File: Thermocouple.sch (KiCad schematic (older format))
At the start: 12 parts, among them U2 MCP3550-60-E/SN, U3 MCP3550-60-E/SN, U4 LM324

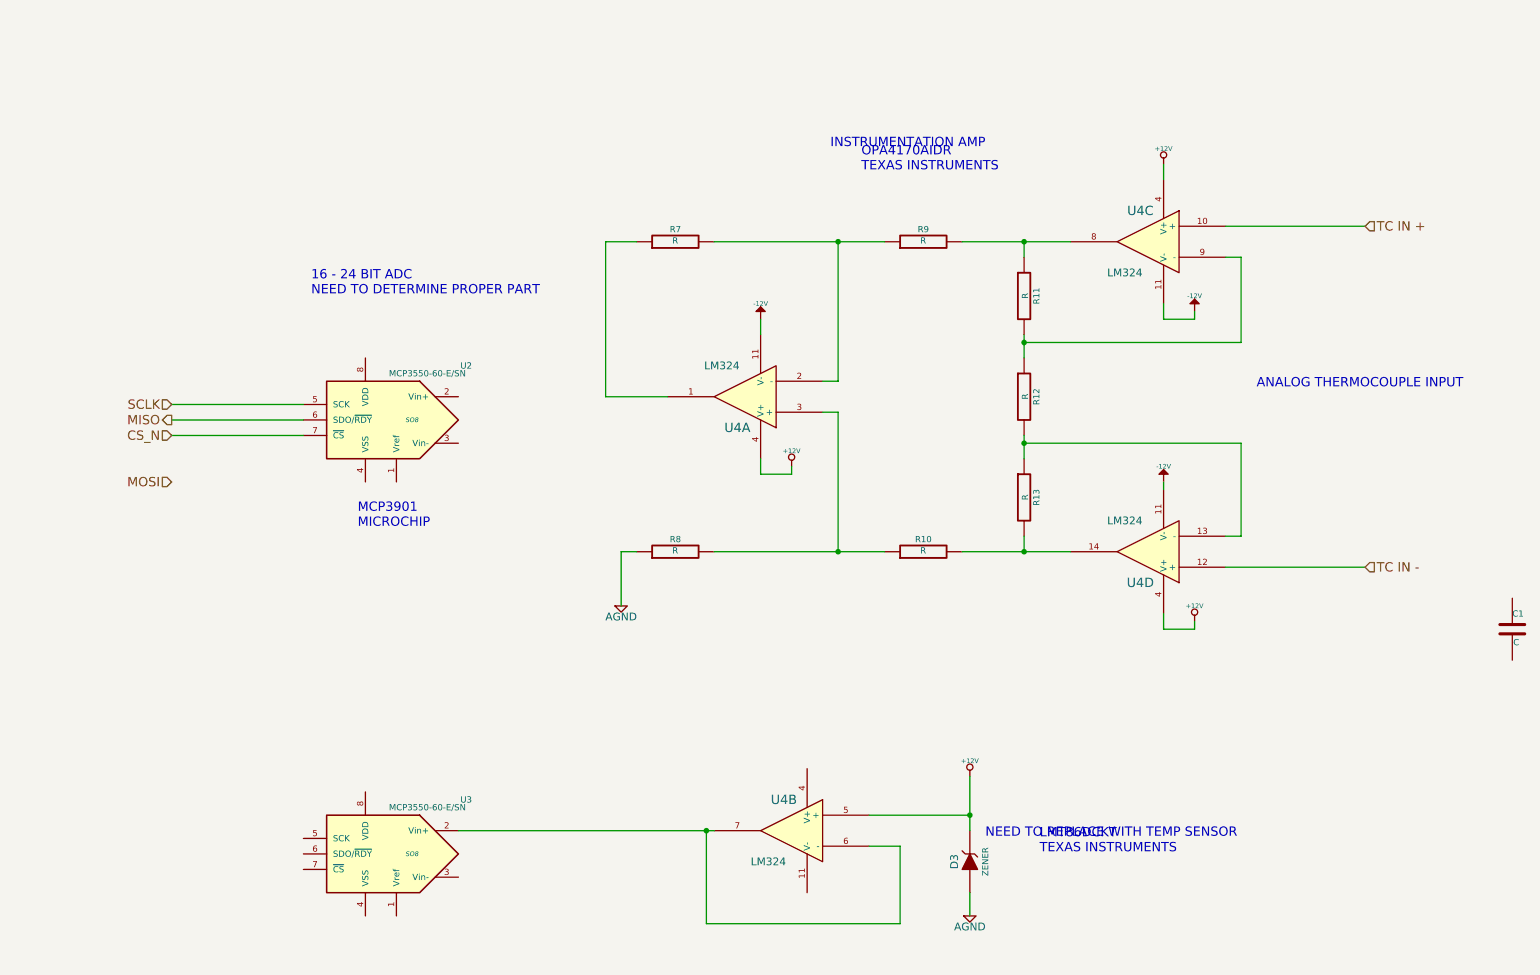
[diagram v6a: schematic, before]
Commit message: worked on associating parts
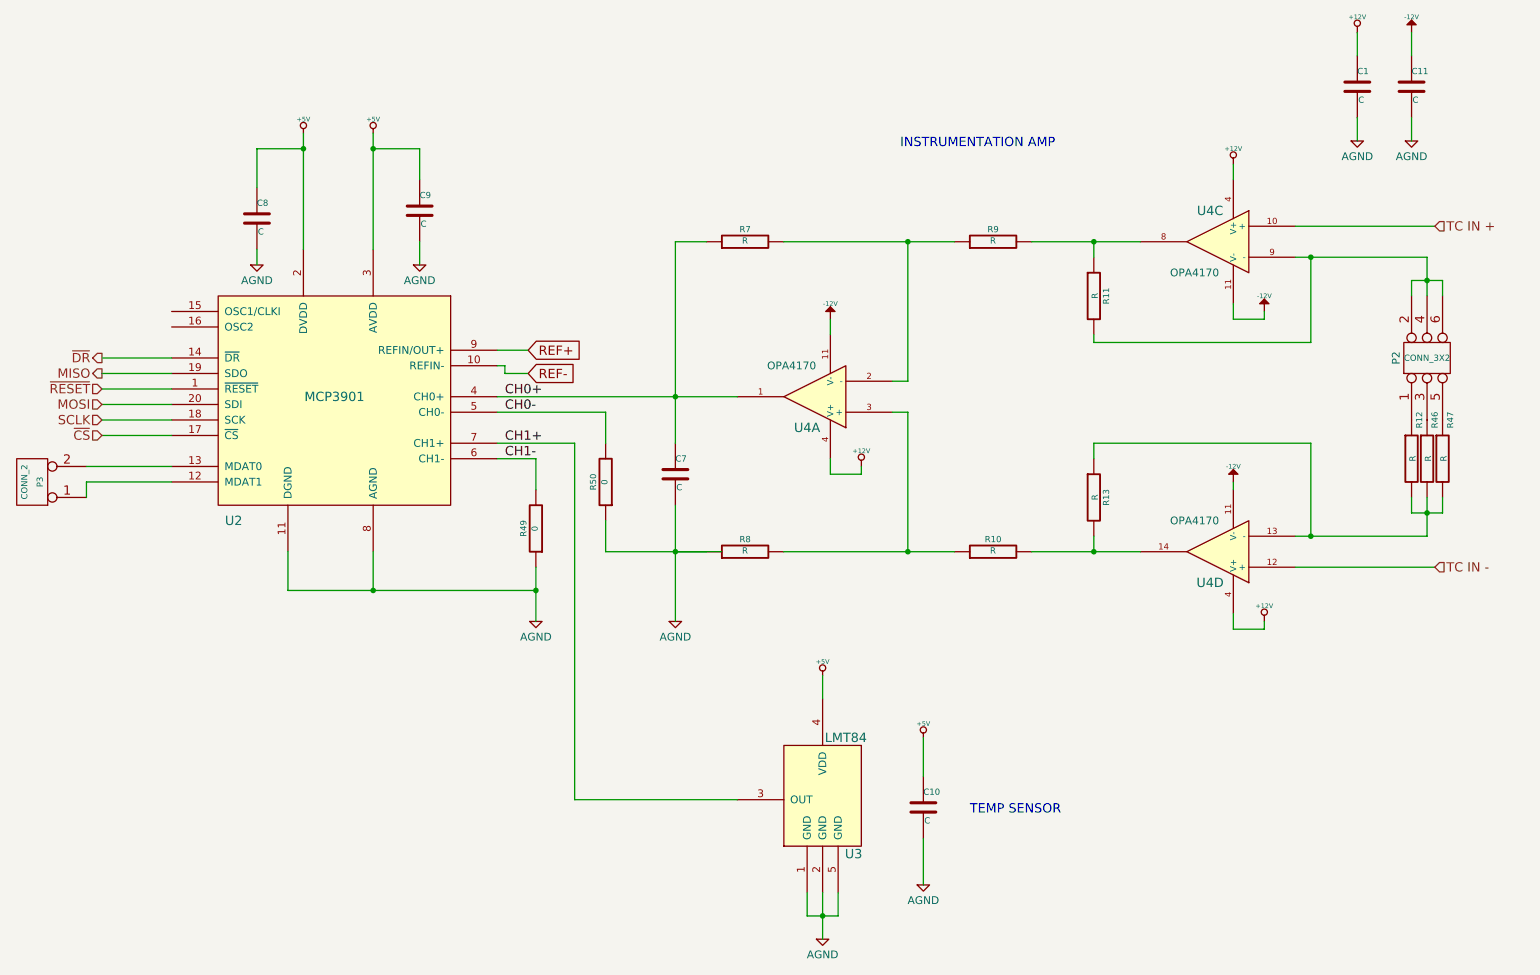
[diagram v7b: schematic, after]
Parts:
- removed D3: ZENER, ~, symbol ZENER
- removed U2, U3: MCP3550-60-E/SN, SO8, symbol MCP3550-60-E/SN
- removed unit 2 of U4
- added C10, C11, C7, C8, C9: C, ~, symbol C
- added P2: CONN_3X2, symbol CONN_3X2
- added P3: CONN_2, symbol CONN_2
- added R46, R47: R, ~, symbol R
- added R49, R50: 0, ~, symbol R
- added U2: MCP3901, symbol MCP3901
- added U3: LMT84, symbol LMT84
- U4: value LM324 -> OPA4170
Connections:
- net +12V: now also C1.1
- net -12V: now also C11.1
- net AGND: now also C1.2, C10.2, C11.2, C7.2, C8.2, C9.2, R49.1, R50.1, U2.11 (DGND), U2.8 (AGND), U3.1 (GND), U3.2 (GND), U3.5 (GND)
- net MISO: now also U2.19 (SDO)
- net MOSI: now also U2.20 (SDI)
- net SCLK: now also U2.18 (SCK)
- net at R11.2, U4.9 (-): now also P2.2, P2.4, P2.6; no longer R12.1
- net at R12.2, R13.1, U4.13 (-): now also R46.2, R47.2
- net CH0+: now reaches R7.1, U4.1
- net CH0+: now also C7.1, U2.4 (CH0+)
- new net: P2.1, R12.1
- new net: P3.1 (P1), U2.12 (MDAT1)
- new net: P3.2 (PM), U2.13 (MDAT0)
- new net: P2.3, R46.1
- new net: P2.5, R47.1
- new net +5V: C10.1, C8.1, C9.1, U2.2 (DVDD), U2.3 (AVDD), U3.4 (VDD)
- new net CH0-: R50.2, U2.5 (CH0-)
- new net CH1+: U2.7 (CH1+), U3.3 (OUT)
- new net CH1-: R49.2, U2.6 (CH1-)
- new net REF+: U2.9 (REFIN/OUT+)
- new net REF-: U2.10 (REFIN-)
- new net ~CS: U2.17 (~CS)
- new net ~DR: U2.14 (~DR)
- new net ~RESET: U2.1 (~RESET)
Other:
- note added: "TEMP SENSOR"
- note removed: "16 - 24 BIT ADC\nNEED TO DETERMINE PROPER PART"
- note removed: "ANALOG THERMOCOUPLE INPUT"
- note removed: "LMT86DCKT\nTEXAS INSTRUMENTS"
- note removed: "MCP3901\nMICROCHIP"
- note removed: "NEED TO REPLACE WITH TEMP SENSOR"
- note removed: "OPA4170AIDR\nTEXAS INSTRUMENTS"
- moved on the sheet: C1, R10, R11, R12, R13, R7, R8, R9, U4A, U4C, U4D
